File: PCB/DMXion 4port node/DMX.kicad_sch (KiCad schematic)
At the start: 45 parts, among them J10 XLR5, J11 XLR3, J4 XLR5, J5 XLR3, J6 XLR5, J7 XLR3, J8 XLR5, J9 XLR3, U10 MAX3485, U11 MAX3485, U12 TXS0101DCK, U8 MAX3485, U9 MAX3485

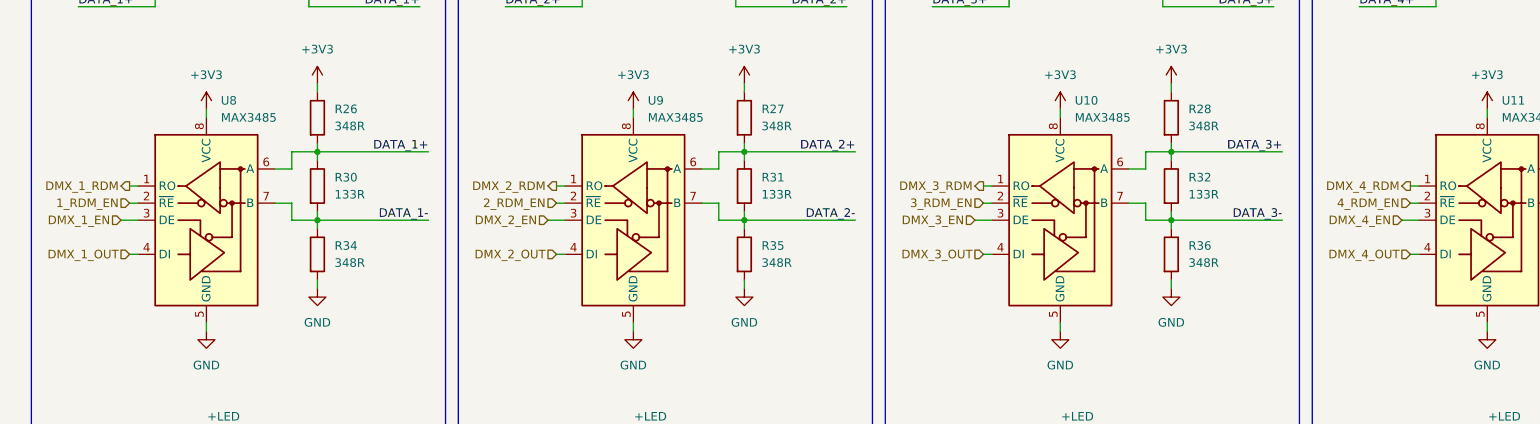
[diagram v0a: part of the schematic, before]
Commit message: Added more testpoints
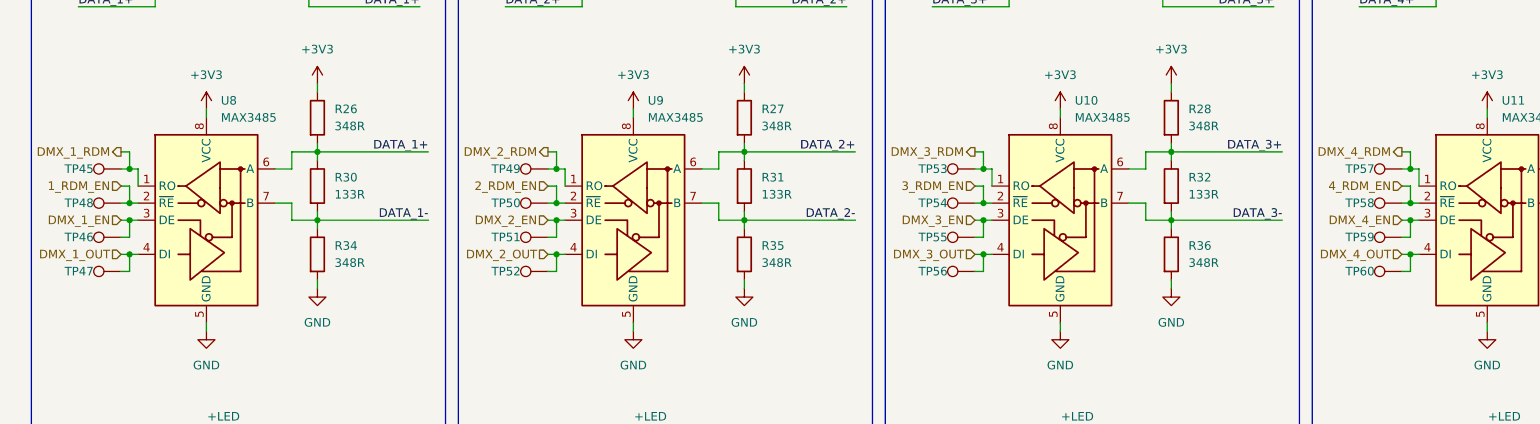
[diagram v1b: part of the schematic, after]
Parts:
- added TP45, TP46, TP47, TP48, TP49, TP50, TP51, TP52, TP53, TP54, TP55, TP56, TP57, TP58, TP59, TP60: TestPoint, TestPoint:TestPoint_Pad_D1.5mm, symbol Connector:TestPoint
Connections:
- net 1_RDM_EN: now also TP48.1
- net 2_RDM_EN: now also TP50.1
- net 3_RDM_EN: now also TP54.1
- net 4_RDM_EN: now also TP58.1
- net DMX_1_EN: now also TP46.1
- net DMX_1_OUT: now also TP47.1
- net DMX_1_RDM: now also TP45.1
- net DMX_2_EN: now also TP51.1
- net DMX_2_OUT: now also TP52.1
- net DMX_2_RDM: now also TP49.1
- net DMX_3_EN: now also TP55.1
- net DMX_3_OUT: now also TP56.1
- net DMX_3_RDM: now also TP53.1
- net DMX_4_EN: now also TP59.1
- net DMX_4_OUT: now also TP60.1
- net DMX_4_RDM: now also TP57.1
